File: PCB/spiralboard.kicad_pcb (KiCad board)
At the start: 2 copper layers, 88.5 x 100 mm, 86 parts, among them J1 Conn_01x05_Pin, J2 Conn_01x02_Pin, SW1 SW_DPDT_x2, U1 ESP-12F

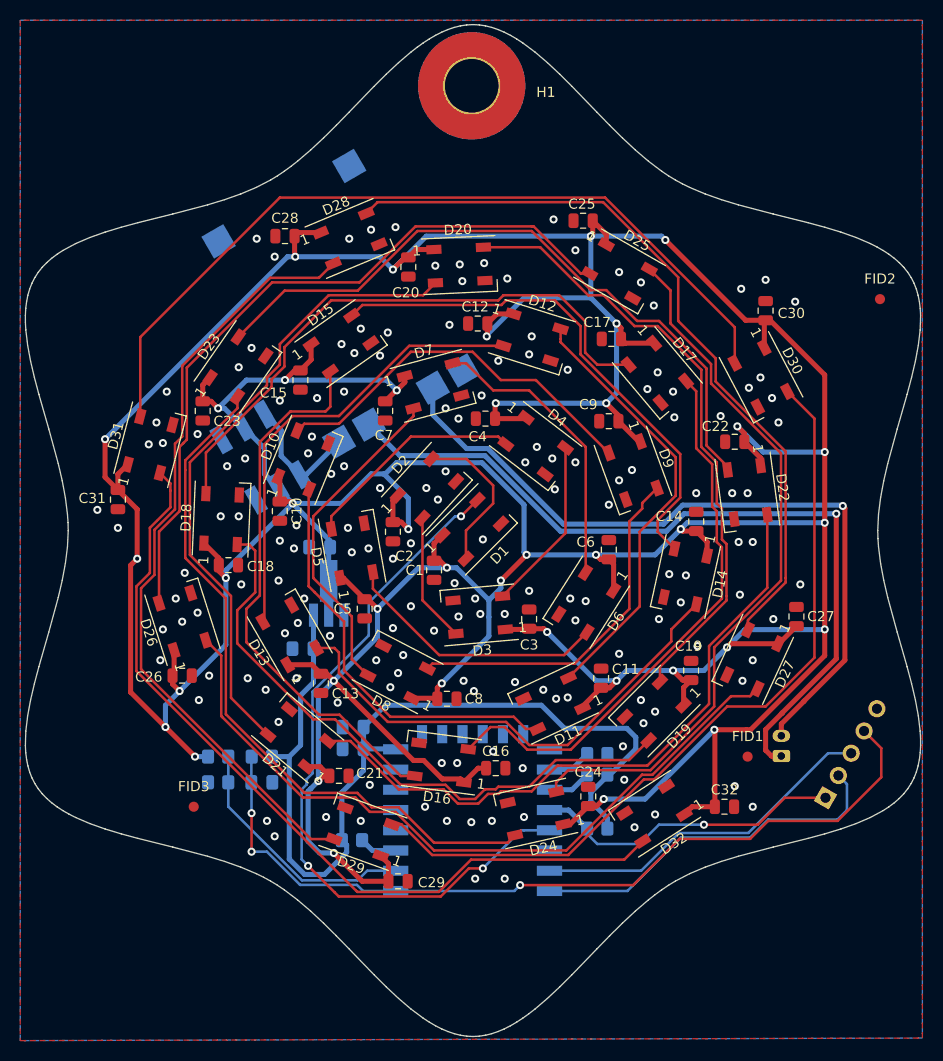
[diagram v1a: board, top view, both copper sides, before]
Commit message: v1.1 commit (mostly for easy hand soldering) - longer pads esp8266 - caps and resistors on bottom changed from 0805 to 1206 - added push button - smaller pads on charger - prevent short circuit - changed LDO to SOT-23 - switched polarity of lipo receptacle
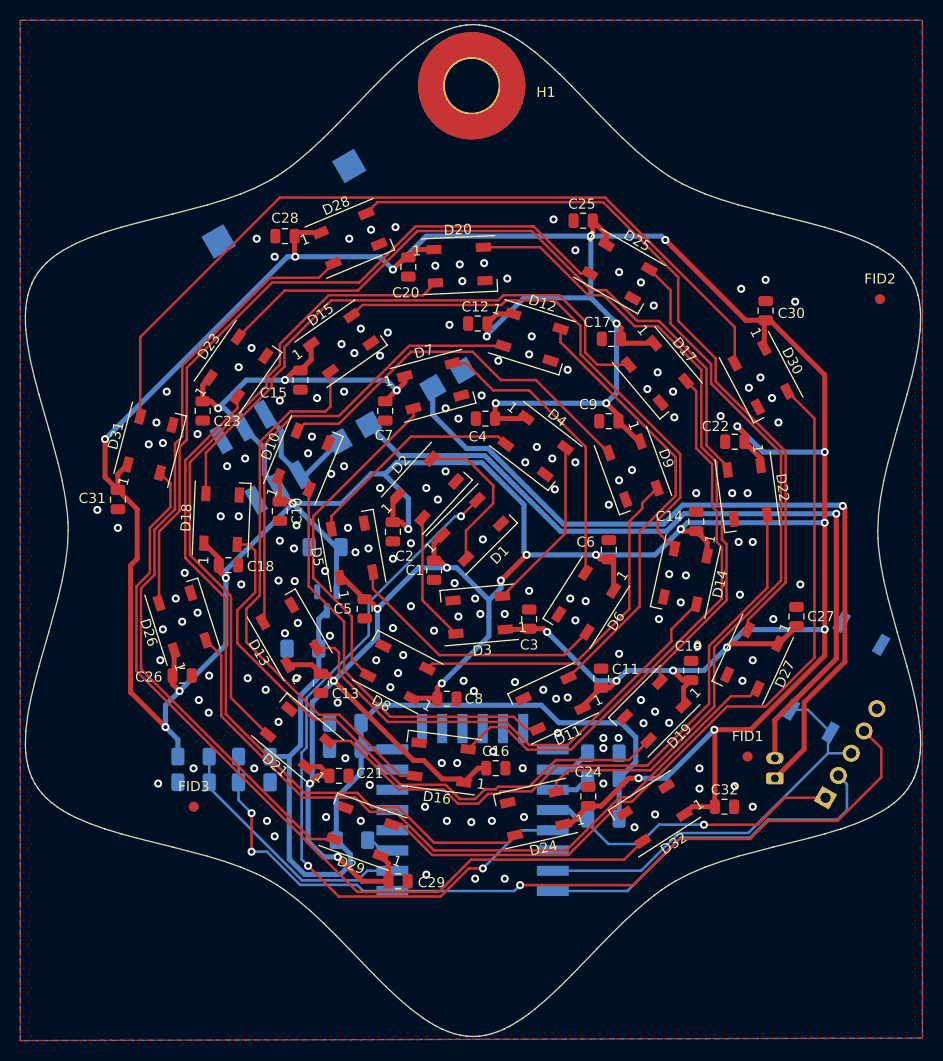
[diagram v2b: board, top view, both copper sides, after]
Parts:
- added SW3: SW_Push_Dual, KH-6X6X6H-STM:KH-6X6X6H-STM, B.Cu at (199.5, 117.0)
- C33, C34, C35, C36, C37: footprint Capacitor_SMD:C_0805_2012Metric_Pad1.18x1.45mm_HandSolder -> Capacitor_SMD:C_1206_3216Metric_Pad1.33x1.80mm_HandSolder
- R1, R2, R3, R4, R5, R6, R7: footprint Resistor_SMD:R_0805_2012Metric_Pad1.20x1.40mm_HandSolder -> Resistor_SMD:R_1206_3216Metric_Pad1.30x1.75mm_HandSolder
- U1: footprint RF_Module:ESP-12E -> ESP12-E_HandSolder:ESP-12E_HandSolder
- U3: footprint Package_TO_SOT_SMD:SOT-89-3_Handsoldering -> Package_TO_SOT_SMD:SOT-23
- moved R2 2.43 mm to (136.0, 124.8)
- moved R3 2.43 mm to (136.0, 127.4)
- moved J2 2.31 mm to (193.4, 127.0)
- moved R5 1.13 mm to (176.5, 131.0)
- moved U3 1.10 mm to (149.2, 109.5), turned to -90 degrees
- moved C35 0.87 mm to (151.0, 121.5)
- moved C34 0.76 mm to (151.0, 124.1)
- moved C33 0.75 mm to (142.0, 127.4)
- moved R4 0.75 mm to (142.0, 124.8)
- moved R7 0.71 mm to (176.5, 127.0)
- moved R6 0.61 mm to (176.5, 124.5)
- moved C37 0.54 mm to (149.0, 104.1)
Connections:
- J2 pad 1: /ESP8266/Bat+ -> /ESP8266/Bat-
- J2 pad 2: /ESP8266/Bat- -> /ESP8266/Bat+
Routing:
- net Net-(J1-Pin_3): track 34.6 -> 41.6 mm
- net /ESP8266/Bat-: track 73.9 -> 78.4 mm
- net VCC: track 632.5 -> 630.1 mm, vias 39 -> 37
- net Net-(U1-EN): track 3.75 -> 2.87 mm
- net Net-(U1-ADC): track 24.9 -> 25.7 mm
- net /ESP8266/Bat+: track 79.5 -> 80.1 mm
- net RESET: track 83.2 -> 83.7 mm
- net GND: vias 163 -> 176
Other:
- board text added: "v1.1 @casartar 2024"
- board text removed: "v1.0 @casartar 2023"
